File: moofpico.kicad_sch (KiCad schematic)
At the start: 22 parts, among them J1 Conn_01x04, J100 Bus_Apple_II_Card_Side, J2 Micro_SD_Card_Det2, Q1 BS170, SW1 SW_DIP_x01, U2 74F11, U3 74LVC245, U4 74LVC245, U5 74LVC245, U6 RaspberryPi_Pico

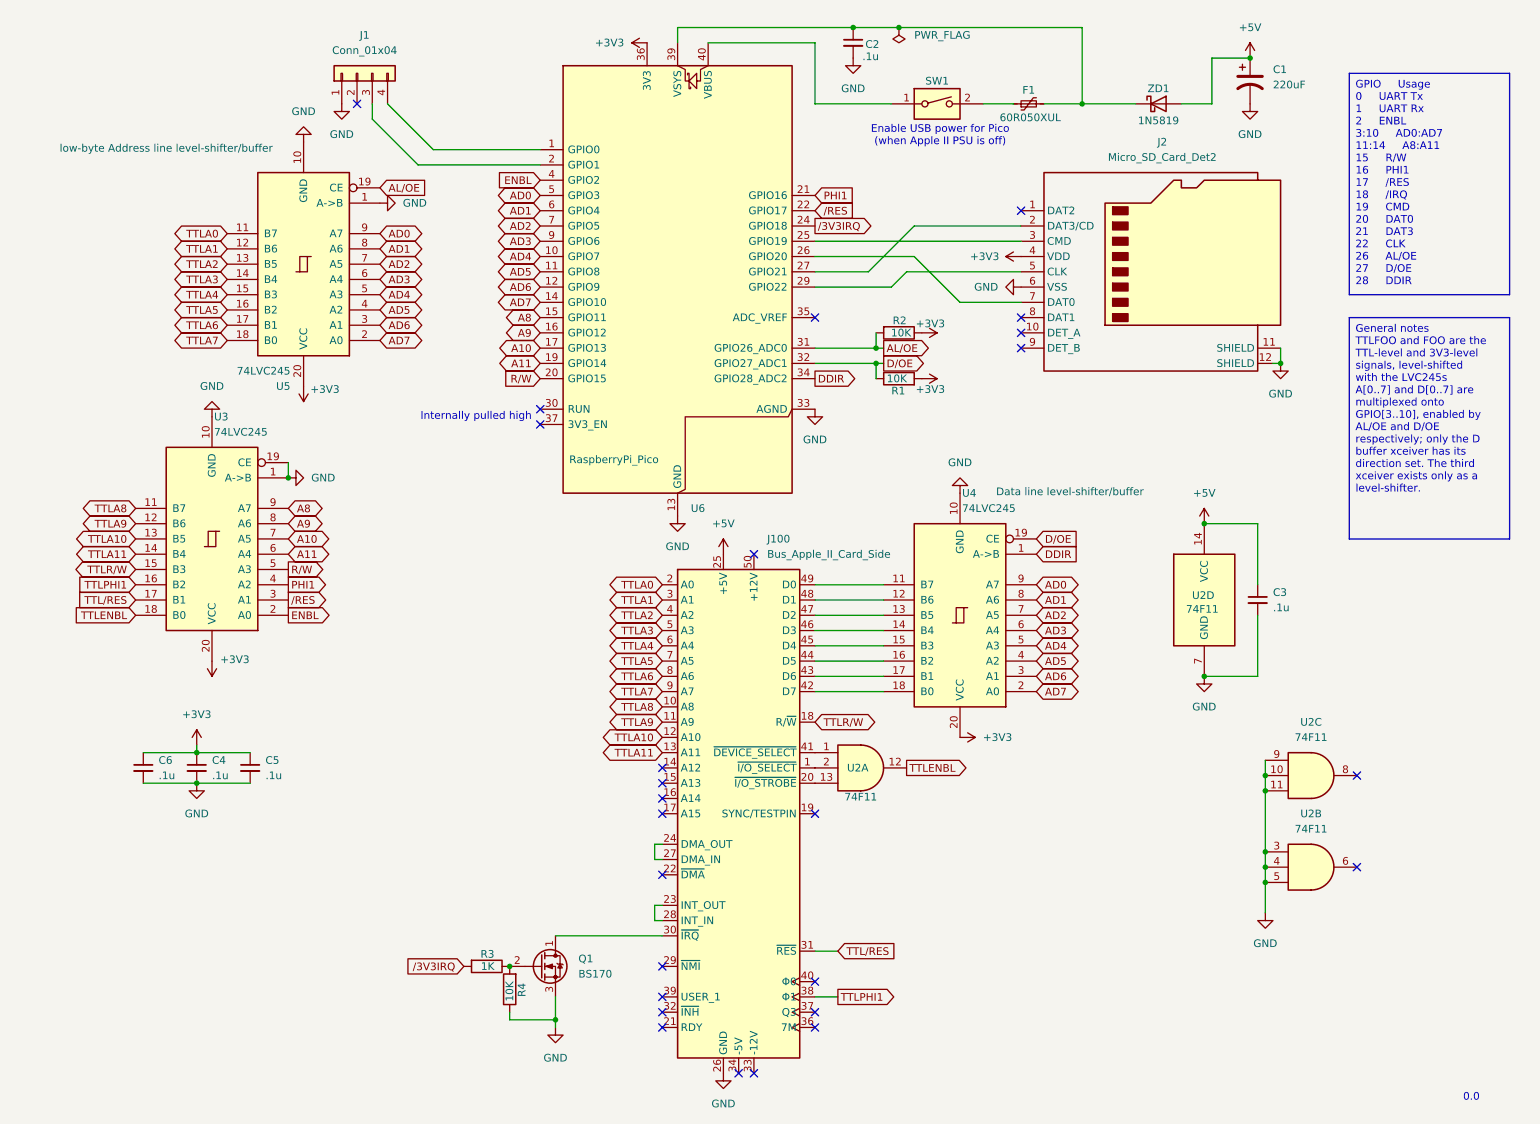
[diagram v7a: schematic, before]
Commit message: major design change: get rid of the uart headers and usb power dip switch I'm not convinced they're actually needed, and the stuff around the USB power in the pico manual makes me think it's superfluous at best
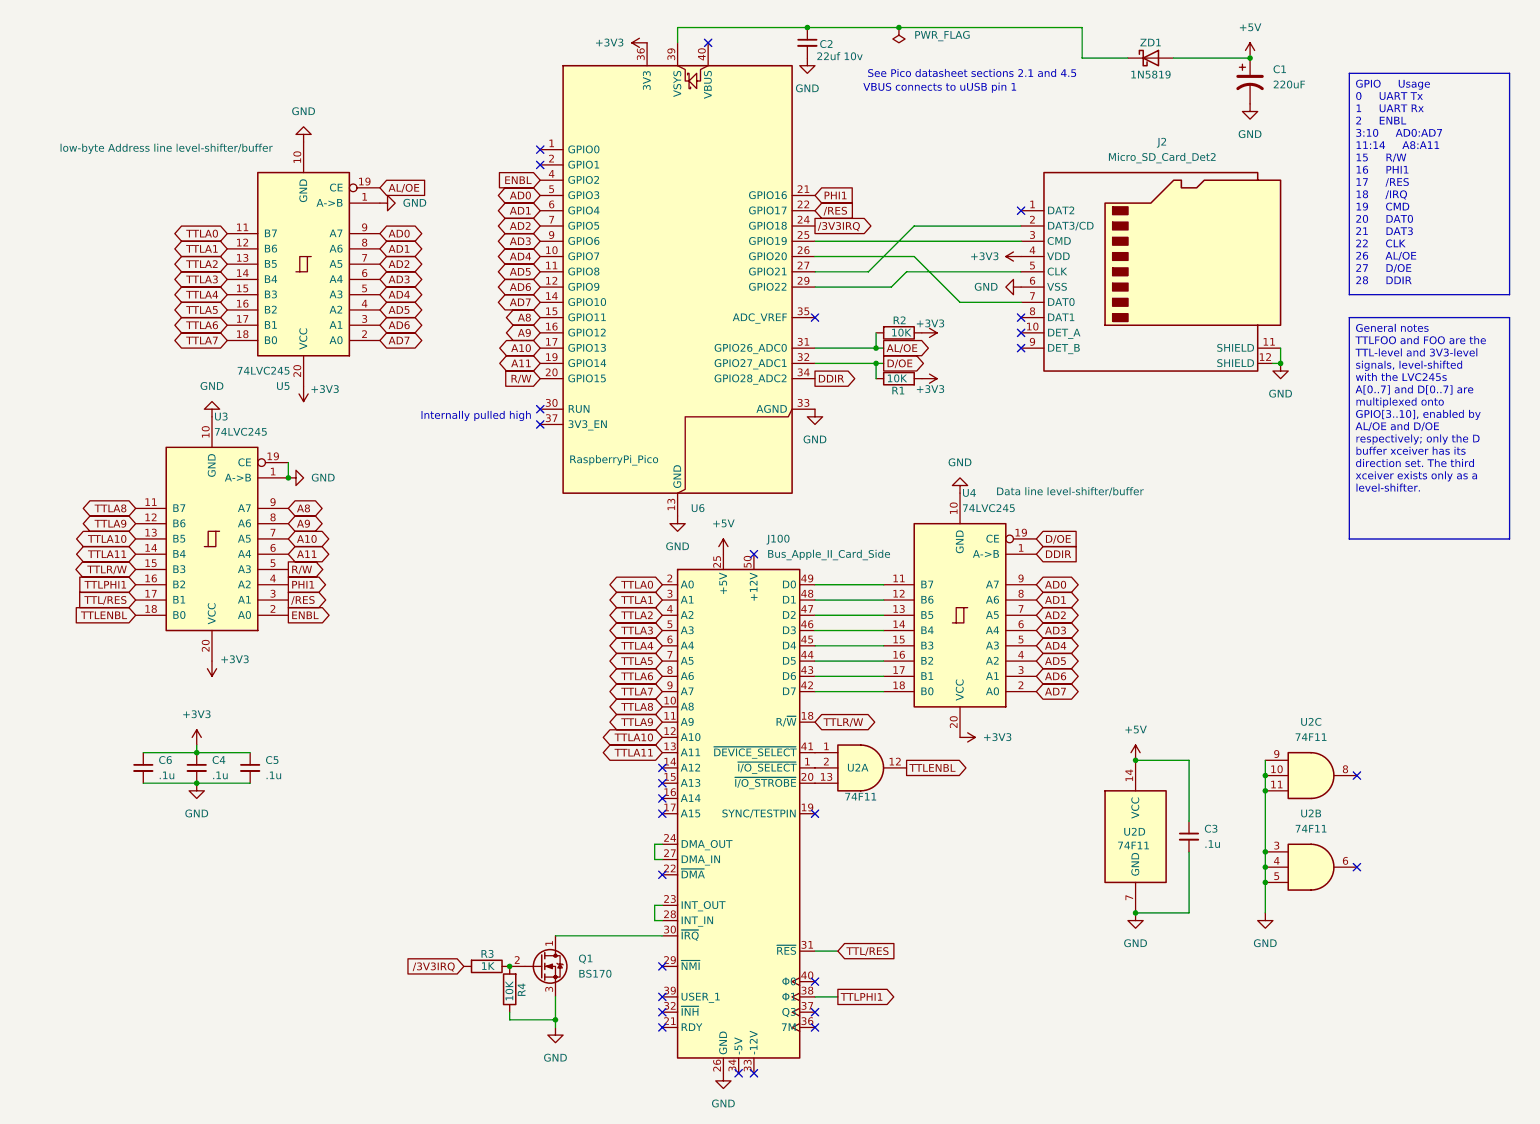
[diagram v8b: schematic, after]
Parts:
- removed F1: 60R050XUL, Fuse:Fuse_BelFuse_0ZRE0005FF_L8.3mm_W3.8mm, symbol Device:Polyfuse_Small
- removed J1: Conn_01x04, Connector_PinHeader_1.27mm:PinHeader_1x04_P1.27mm_Vertical, symbol Connector_Generic:Conn_01x04
- removed SW1: SW_DIP_x01, Button_Switch_THT:SW_DIP_SPSTx01_Slide_6.7x4.1mm_W7.62mm_P2.54mm_LowProfile, symbol Switch:SW_DIP_x01
- C2: value .1u -> 22uf 10v; footprint Capacitor_THT:C_Disc_D3.8mm_W2.6mm_P2.50mm -> Capacitor_THT:C_Disc_D5.0mm_W2.5mm_P2.50mm
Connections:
- no-connect marks 26 -> 28
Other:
- note added: "See Pico datasheet sections 2.1 and 4.5"
- note added: "VBUS connects to uUSB pin 1"
- note removed: "0.0"
- note removed: "Enable USB power for Pico (when Apple II PSU is off)"
- moved on the sheet: C2, C3, U2D, ZD1
